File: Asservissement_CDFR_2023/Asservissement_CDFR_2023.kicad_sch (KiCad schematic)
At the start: 113 parts, among them IC1 A3930KJPTR-T, IC2 A3930KJPTR-T, J1 Connecteur batterie, J10 Free Connecteur, J11 Conn_01x02, J12 Conn_01x02, J13 Connecteur Odométrie, J2 Conn_01x03, J3 Conn_01x05, J4 Connecteur Programmation, J5 Conn_01x03, J6 Connecteur Odométrie, J7 Conn_01x03, J8 Conn_01x03, J9 Conn_01x05, Q1 QM6006D, Q10 QM6006D, Q11 QM6006D, Q12 QM6006D, Q13 Q_NMOS_GDS, Q2 QM6006D, Q3 QM6006D, Q4 QM6006D, Q5 QM6006D, Q6 QM6006D, Q7 QM6006D, Q8 QM6006D, Q9 QM6006D, U1 LM317_SOT-223, U2 TPS562200, U3 STM32F401RCTx, Y1 Crystal_GND24

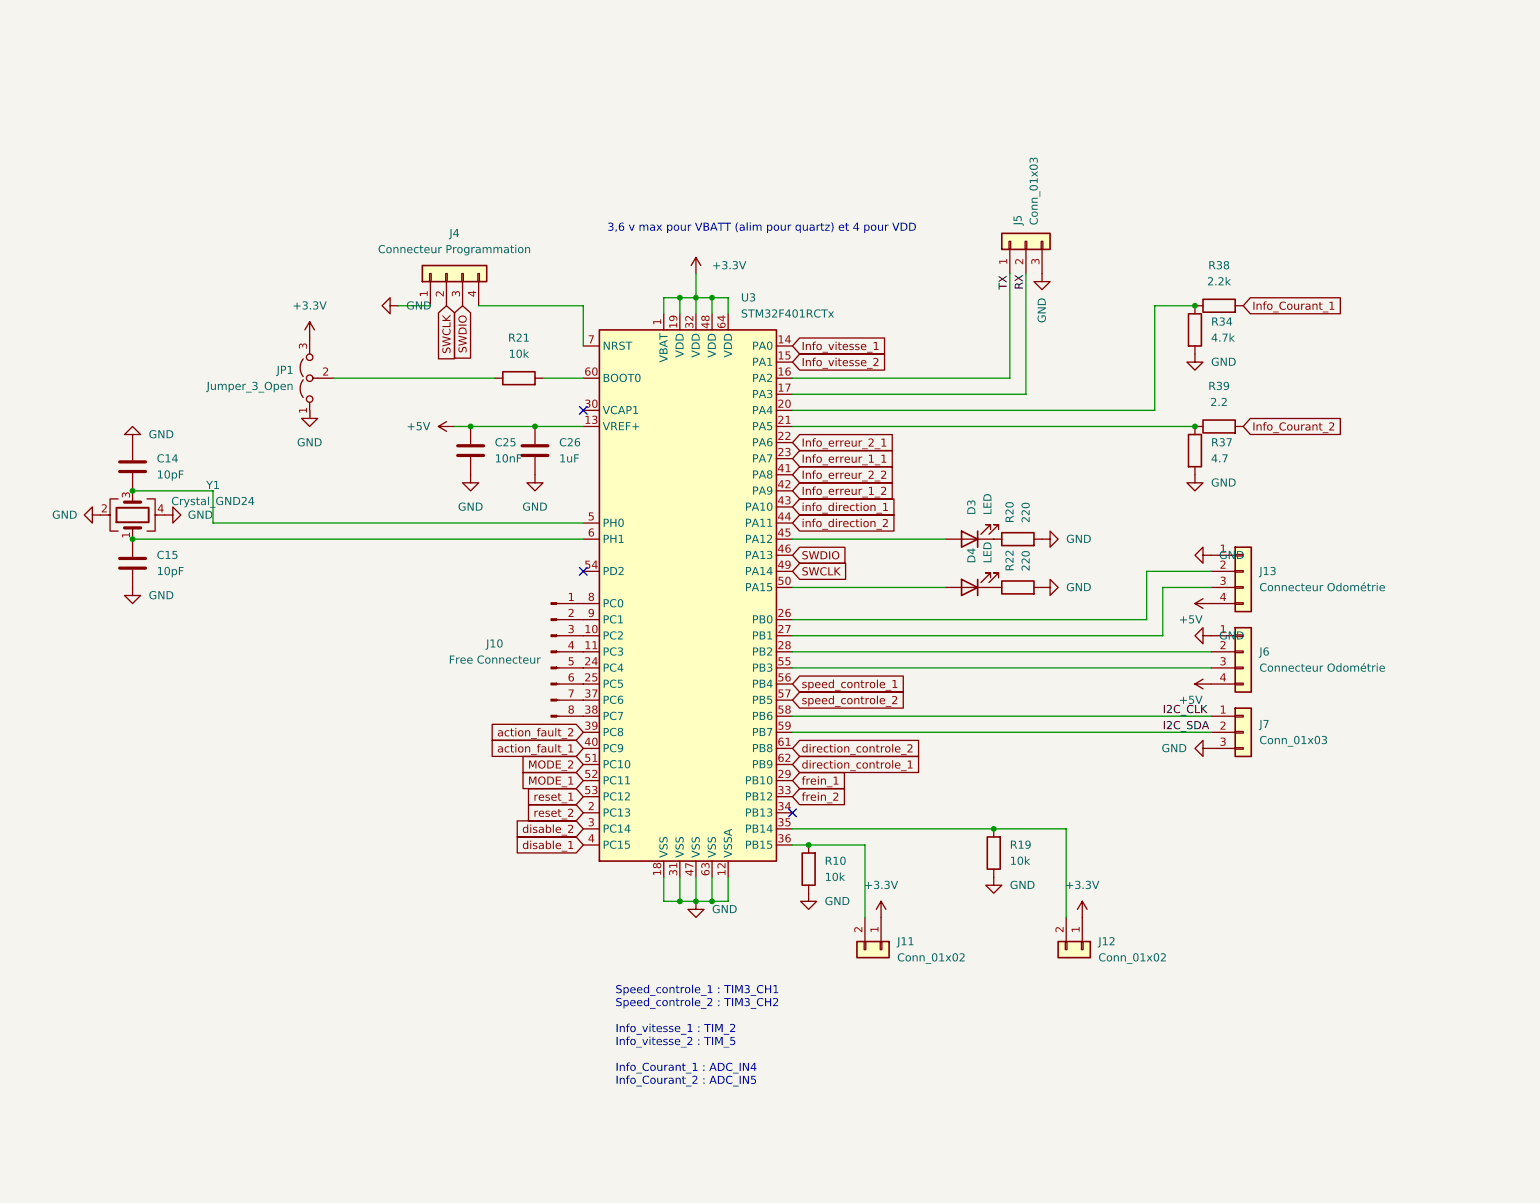
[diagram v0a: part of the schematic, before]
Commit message: uController modification pinout
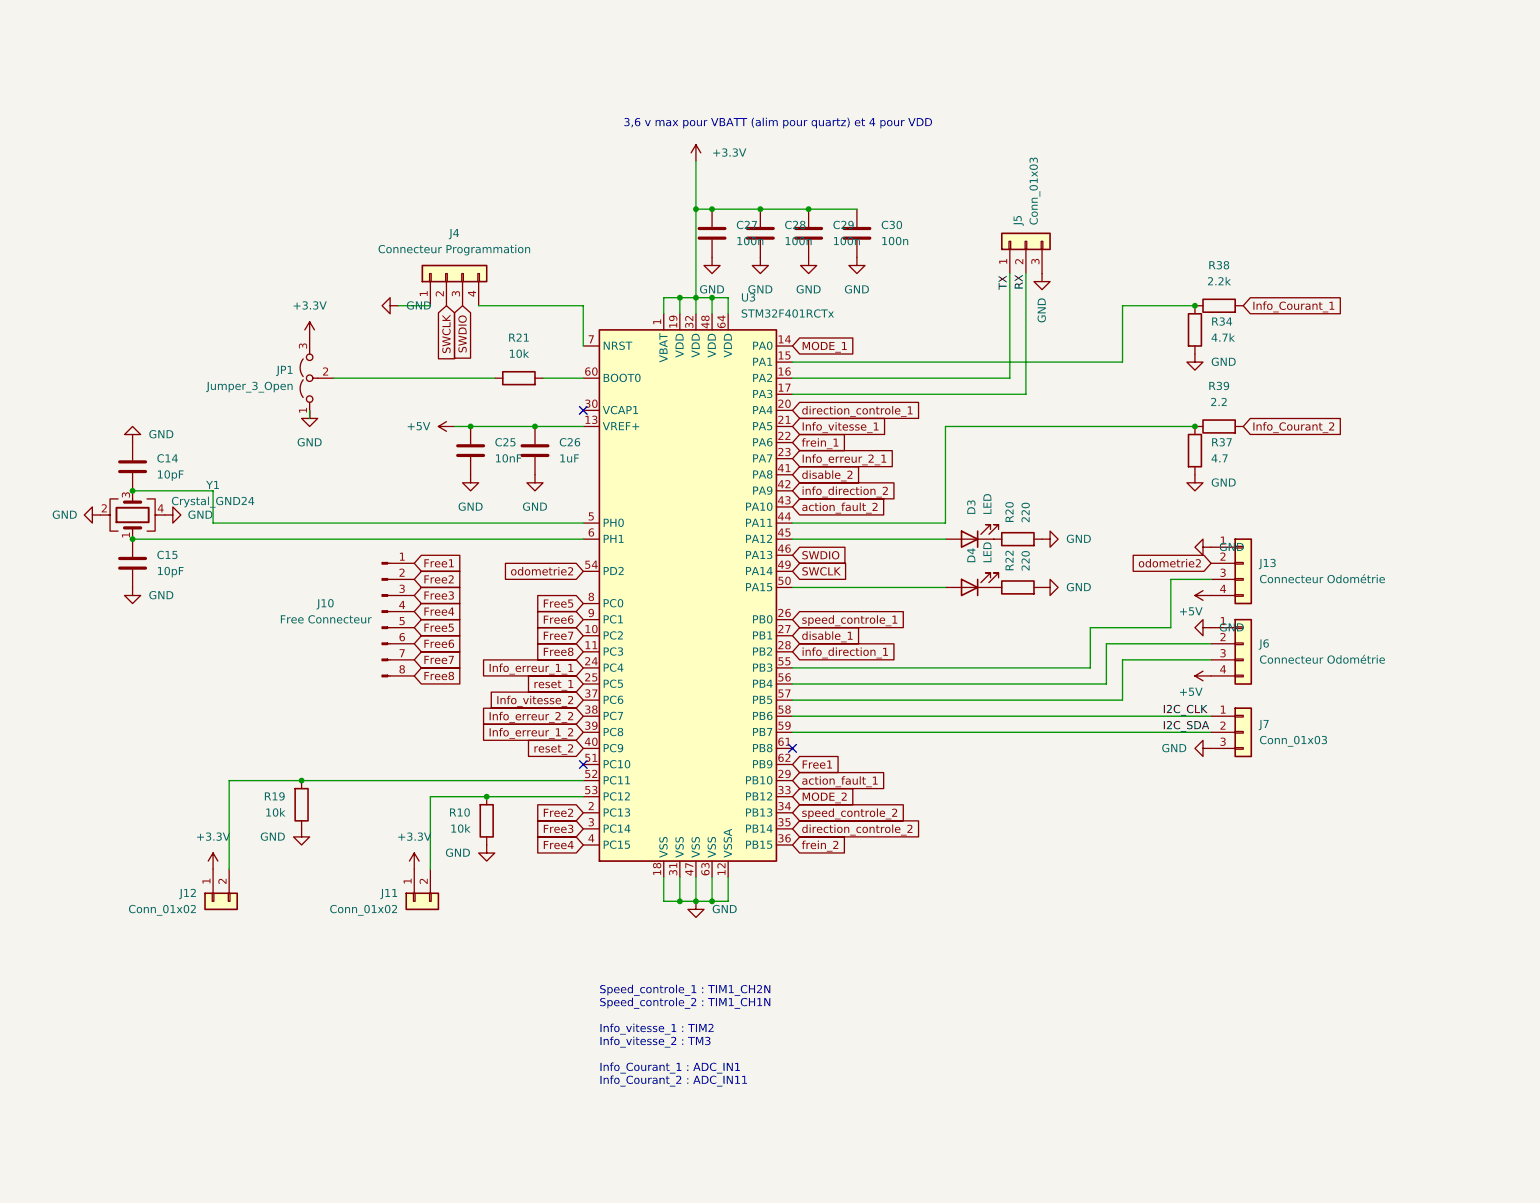
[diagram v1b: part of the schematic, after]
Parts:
- added C27, C28, C29, C30: 100n, Capacitor_SMD:C_0805_2012Metric_Pad1.18x1.45mm_HandSolder, symbol Device:C
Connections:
- net +3.3V: now also C27.1, C28.1, C29.1, C30.1
- net GND: now also C27.2, C28.2, C29.2, C30.2
- net Info_erreur_1_1: now also U3.24 (PC4); no longer U3.23 (PA7)
- net Info_erreur_1_2: now also U3.39 (PC8); no longer U3.42 (PA9)
- net Info_erreur_2_1: now also U3.23 (PA7); no longer U3.22 (PA6)
- net Info_erreur_2_2: now also U3.38 (PC7); no longer U3.41 (PA8)
- net Info_vitesse_1: now also U3.21 (PA5); no longer U3.14 (PA0)
- net Info_vitesse_2: now also U3.37 (PC6); no longer U3.15 (PA1)
- net MODE_1: now also U3.14 (PA0); no longer U3.52 (PC11)
- net MODE_2: now also U3.33 (PB12); no longer U3.51 (PC10)
- net action_fault_1: now also U3.29 (PB10); no longer U3.40 (PC9)
- net action_fault_2: now also U3.43 (PA10); no longer U3.39 (PC8)
- net direction_controle_1: now also U3.20 (PA4); no longer U3.62 (PB9)
- net direction_controle_2: now also U3.35 (PB14); no longer U3.61 (PB8)
- net disable_1: now also U3.27 (PB1); no longer U3.4 (PC15)
- net disable_2: now also U3.41 (PA8); no longer U3.3 (PC14)
- net frein_1: now also U3.22 (PA6); no longer U3.29 (PB10)
- net frein_2: now also U3.36 (PB15); no longer U3.33 (PB12)
- net info_direction_1: now also U3.28 (PB2); no longer U3.43 (PA10)
- net info_direction_2: now also U3.42 (PA9); no longer U3.44 (PA11)
- net reset_1: now also U3.25 (PC5); no longer U3.53 (PC12)
- net reset_2: now also U3.40 (PC9); no longer U3.2 (PC13)
- net speed_controle_1: now also U3.26 (PB0); no longer U3.56 (PB4)
- net speed_controle_2: now also U3.34 (PB13); no longer U3.57 (PB5)
- net odometrie2: now reaches J13.2 (Pin_2)
- net odometrie2: now also U3.54 (PD2); no longer U3.26 (PB0)
- net at J13.3 (Pin_3): now also U3.55 (PB3); no longer U3.27 (PB1)
- net at J12.2 (Pin_2), R19.2: now also U3.52 (PC11); no longer U3.35 (PB14)
- net Free3: now reaches J10.3 (Pin_3)
- net Free3: now also U3.3 (PC14); no longer U3.10 (PC2)
- net Free4: now reaches J10.4 (Pin_4)
- net Free4: now also U3.4 (PC15); no longer U3.11 (PC3)
- net at R34.1, R38.1: now also U3.15 (PA1); no longer U3.20 (PA4)
- net at R37.1, R39.1: now also U3.44 (PA11); no longer U3.21 (PA5)
- net Free5: now reaches J10.5 (Pin_5)
- net Free5: now also U3.8 (PC0); no longer U3.24 (PC4)
- net Free6: now reaches J10.6 (Pin_6)
- net Free6: now also U3.9 (PC1); no longer U3.25 (PC5)
- net at J6.2 (Pin_2): now also U3.56 (PB4); no longer U3.28 (PB2)
- net at J11.2 (Pin_2), R10.2: now also U3.53 (PC12); no longer U3.36 (PB15)
- net Free7: now reaches J10.7 (Pin_7)
- net Free7: now also U3.10 (PC2); no longer U3.37 (PC6)
- net Free8: now reaches J10.8 (Pin_8)
- net Free8: now also U3.11 (PC3); no longer U3.38 (PC7)
- net at J6.3 (Pin_3): now also U3.57 (PB5); no longer U3.55 (PB3)
- net Free1: now reaches J10.1 (Pin_1)
- net Free1: now also U3.62 (PB9); no longer U3.8 (PC0)
- net Free2: now reaches J10.2 (Pin_2)
- net Free2: now also U3.2 (PC13); no longer U3.9 (PC1)
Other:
- note added: "Speed_controle_1 : TIM1_CH2N Speed_controle_2 : TIM1_CH1N Info_vitesse_1 : TIM2 Info_vitesse_2 : TM3 Info_Courant_1 : ADC_IN1 Info_Courant_2 : ADC_IN11"
- note removed: "Speed_controle_1 : TIM3_CH1 Speed_controle_2 : TIM3_CH2 Info_vitesse_1 : TIM_2 Info_vitesse_2 : TIM_5 Info_Courant_1 : ADC_IN4 Info_Courant_2 : ADC_IN5"
- moved on the sheet: J10, J11, J12, J13, J6, R10, R19

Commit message: capacitor error
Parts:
- removed C30: 100n, Capacitor_SMD:C_0805_2012Metric_Pad1.18x1.45mm_HandSolder, symbol Device:C
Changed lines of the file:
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@@
   (junction (at 177.8 29.21) (diameter 0) (color 0 0 0 0)
   )
-  (junction (at 160.02 168.91) (diameter 0) (color 0 0 0 0)
-  )
   (junction (at 468.63 31.75) (diameter 0) (color 0 0 0 0)
   )
@@
     (stroke (width 0) (type default) (color 0 0 0 0))
   )
-  (wire (pts (xy 160.02 168.91) (xy 167.64 168.91))
-    (stroke (width 0) (type default) (color 0 0 0 0))
-  )
   (wire (pts (xy 416.56 307.34) (xy 416.56 320.04))
     (stroke (width 0) (type default) (color 0 0 0 0))
@@
     (pin "4")
   )
-  (symbol (lib_id "Device:C") (at 167.64 172.72 0) (unit 1)
-    (in_bom yes) (on_board yes) (fields_autoplaced)
-    (property "Reference" "C30" (id 0) (at 171.45 171.4499 0)
-      (effects (font (size 1.27 1.27)) (justify left))
-    )
-    (property "Value" "100n" (id 1) (at 171.45 173.9899 0)
-      (effects (font (size 1.27 1.27)) (justify left))
-    )
-    (property "Footprint" "Capacitor_SMD:C_0805_2012Metric_Pad1.18x1.45mm_HandSolder" (id 2) (at 168.6052 176.53 0)
-      (effects (font (size 1.27 1.27)) hide)
-    )
-    (property "Datasheet" "~" (id 3) (at 167.64 172.72 0)
-      (effects (font (size 1.27 1.27)) hide)
-    )
-    (pin "1")
-    (pin "2")
-  )
   (symbol (lib_id "power:GND") (at 450.85 157.48 0) (unit 1)
     (in_bom yes) (on_board yes) (fields_autoplaced)
@@
     (pin "2")
   )
-  (symbol (lib_id "power:GND") (at 167.64 176.53 0) (unit 1)
-    (in_bom yes) (on_board yes) (fields_autoplaced)
-    (property "Reference" "#PWR0101" (id 0) (at 167.64 182.88 0)
-      (effects (font (size 1.27 1.27)) hide)
-    )
-    (property "Value" "GND" (id 1) (at 167.64 181.61 0))
-    (property "Footprint" "" (id 2) (at 167.64 176.53 0)
-      (effects (font (size 1.27 1.27)) hide)
-    )
-    (property "Datasheet" "" (id 3) (at 167.64 176.53 0)
-      (effects (font (size 1.27 1.27)) hide)
-    )
-    (pin "1")
-  )
   (symbol (lib_id "Device:R") (at 359.41 87.63 90) (unit 1)
     (in_bom yes) (on_board yes)
@@
       (reference "#PWR075") (unit 1) (value "GND") (footprint "")
     )
-    (path "/15860844-5217-4f75-a3ad-a7eb0b806d84"
-      (reference "#PWR0101") (unit 1) (value "GND") (footprint "")
-    )
     (path "/a95909f7-bbcb-4f7f-9e42-295067e72c9e"
       (reference "#PWR0102") (unit 1) (value "GND") (footprint "")
@@
       (reference "C29") (unit 1) (value "100n") (footprint "Capacitor_SMD:C_0805_2012Metric_Pad1.18x1.45mm_HandSolder")
     )
-    (path "/0f66cf1e-55a2-4c88-9ff2-d7043d3fb7eb"
-      (reference "C30") (unit 1) (value "100n") (footprint "Capacitor_SMD:C_0805_2012Metric_Pad1.18x1.45mm_HandSolder")
-    )
     (path "/5f822638-2177-4cf9-b5cf-511b4315b4cc"

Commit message: capacitor error
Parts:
- added C30: 100n, Capacitor_SMD:C_0805_2012Metric_Pad1.18x1.45mm_HandSolder, symbol Device:C
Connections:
- net +3.3V: now also C30.1
- net GND: now also C30.2
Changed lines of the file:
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@@
   (junction (at 119.38 46.99) (diameter 0) (color 0 0 0 0)
   )
+  (junction (at 160.02 168.91) (diameter 0) (color 0 0 0 0)
+  )
   (junction (at 468.63 238.76) (diameter 0) (color 0 0 0 0)
   )
@@
     (stroke (width 0) (type default) (color 0 0 0 0))
   )
+  (wire (pts (xy 160.02 168.91) (xy 167.64 168.91))
+    (stroke (width 0) (type default) (color 0 0 0 0))
+  )
   (wire (pts (xy 111.76 29.21) (xy 119.38 29.21))
     (stroke (width 0) (type default) (color 0 0 0 0))
@@
     (pin "3")
   )
+  (symbol (lib_id "power:GND") (at 167.64 176.53 0) (unit 1)
+    (in_bom yes) (on_board yes) (fields_autoplaced)
+    (property "Reference" "#PWR01" (id 0) (at 167.64 182.88 0)
+      (effects (font (size 1.27 1.27)) hide)
+    )
+    (property "Value" "GND" (id 1) (at 167.64 181.61 0))
+    (property "Footprint" "" (id 2) (at 167.64 176.53 0)
+      (effects (font (size 1.27 1.27)) hide)
+    )
+    (property "Datasheet" "" (id 3) (at 167.64 176.53 0)
+      (effects (font (size 1.27 1.27)) hide)
+    )
+    (pin "1")
+  )
   (symbol (lib_id "Device:R") (at 193.04 228.6 90) (unit 1)
     (in_bom yes) (on_board yes) (fields_autoplaced)
@@
     (pin "2")
   )
+  (symbol (lib_id "Device:C") (at 167.64 172.72 0) (unit 1)
+    (in_bom yes) (on_board yes) (fields_autoplaced)
+    (property "Reference" "C30" (id 0) (at 171.45 171.4499 0)
+      (effects (font (size 1.27 1.27)) (justify left))
+    )
+    (property "Value" "100n" (id 1) (at 171.45 173.9899 0)
+      (effects (font (size 1.27 1.27)) (justify left))
+    )
+    (property "Footprint" "Capacitor_SMD:C_0805_2012Metric_Pad1.18x1.45mm_HandSolder" (id 2) (at 168.6052 176.53 0)
+      (effects (font (size 1.27 1.27)) hide)
+    )
+    (property "Datasheet" "~" (id 3) (at 167.64 172.72 0)
+      (effects (font (size 1.27 1.27)) hide)
+    )
+    (pin "1")
+    (pin "2")
+  )
   (symbol (lib_id "Device:R") (at 457.2 102.87 90) (unit 1)
     (in_bom yes) (on_board yes) (fields_autoplaced)
@@
       (reference "#FLG0104") (unit 1) (value "PWR_FLAG") (footprint "")
     )
+    (path "/993b99c0-00b2-4cc6-ad95-47838cc56e2d"
+      (reference "#PWR01") (unit 1) (value "GND") (footprint "")
+    )
     (path "/a1722b98-9caa-4037-980c-f546f9693881"
       (reference "#PWR02") (unit 1) (value "+5V") (footprint "")
@@
       (reference "C29") (unit 1) (value "100n") (footprint "Capacitor_SMD:C_0805_2012Metric_Pad1.18x1.45mm_HandSolder")
     )
+    (path "/d8d1214a-5385-4967-bb89-b842f650c07d"
+      (reference "C30") (unit 1) (value "100n") (footprint "Capacitor_SMD:C_0805_2012Metric_Pad1.18x1.45mm_HandSolder")
+    )
     (path "/5f822638-2177-4cf9-b5cf-511b4315b4cc"

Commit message: Routing almost done
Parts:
- added H1, H2, H3, H4: MountingHole_Pad, MountingHole:MountingHole_3.2mm_M3_Pad_Via, symbol Mechanical:MountingHole_Pad
- added H5, H6, H7, H8: MountingHole_Pad, MountingHole:MountingHole_2.7mm_Pad_Via, symbol Mechanical:MountingHole_Pad
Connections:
- net +3.3V: now also C25.1, C26.1, U3.13 (VREF+)
- net +5V: no longer C25.1, C26.1, U3.13 (VREF+)
- net GND: now also H1.1, H2.1, H3.1, H4.1, H5.1, H6.1, H7.1, H8.1

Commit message: Fix Boost converter
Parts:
- removed C10, C7: 220u, Capacitor_SMD:CP_Elec_10x10.5, symbol Device:C_Polarized
- removed C8: 100nF, Capacitor_SMD:C_0805_2012Metric_Pad1.18x1.45mm_HandSolder, symbol Device:C
- removed L1: MDA4020-3R3M, Inductor_SMD:L_Vishay_IFSC-1515AH_4x4x1.8mm, symbol Device:L
- removed R1: 1k, Resistor_SMD:R_0805_2012Metric_Pad1.20x1.40mm_HandSolder, symbol Device:R
- removed R8: 3.3k, Resistor_SMD:R_0805_2012Metric_Pad1.20x1.40mm_HandSolder, symbol Device:R
- removed U2: TPS562200, Package_TO_SOT_SMD:SOT-23-6, symbol Regulator_Switching:TPS562200
- added C31, C33: 220uF, Capacitor_SMD:CP_Elec_10x10.5, symbol Device:C_Polarized
- added C32: 100nF, Capacitor_SMD:C_0805_2012Metric_Pad1.18x1.45mm_HandSolder, symbol Device:C
- added D6: DIODE, B170B:DIOM505270X240, symbol pspice:DIODE
- added L2: 10uH, IHLP2525CZER100M01:IND_IHLP_2525_CZ-M, symbol Device:L
- added R43: 56k, Resistor_SMD:R_0805_2012Metric, symbol Device:R
- added R44: 10k, Resistor_SMD:R_0805_2012Metric, symbol Device:R
- added U4: LMR16020PDDA, Package_SO:SOIC-8-1EP_3.9x4.9mm_P1.27mm_EP2.41x3.3mm, symbol LMR16020PDDA:LMR16020PDDA
- C11: value 100u -> 100uF
- C27, C28, C29, C30: value 100n -> 100nF
- R11, R12, R13, R26, R27, R28: value R -> 52k
- R37: value 4.7 -> 4.7k
- R39: value 2.2 -> 2.2k
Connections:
- net +5V: now also C33.1, L2.2
- net +BATT: now also C31.1, U4.2 (VIN), U4.3 (EN)
- net GND: now also C31.2, C33.2, D6.1 (K), R44.2, U4.7 (GND)
- new net: C32.1, U4.1 (BOOT)
- new net: C32.2, D6.2 (A), L2.1, R43.1, U4.8 (SW)
- new net: R43.2, R44.1, U4.5 (FB)
- no-connect marks 17 -> 19
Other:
- moved on the sheet: C11, D1, D2, D5, H1, H2, H3, H4, H5, H6, H7, H8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
